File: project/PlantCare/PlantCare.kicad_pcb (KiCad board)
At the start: 4 copper layers, 45.5 x 22.5 mm, 41 parts, among them J1 TFT_0.96_13, J2 TTL-connect-pin4, J3 usbc, J4 Conn_01x02_Female, J5 Conn_01x01_Female, Q1 S8050, Q2 S8050, Q3 S8050, Q4 Q_NMOS_GSD, SW1 SW_DPDT_x2, SW2 SW_Push, SW3 SW_Push, U1 AMS1117-3.3, U2 ESP-12E, U3 CH340C

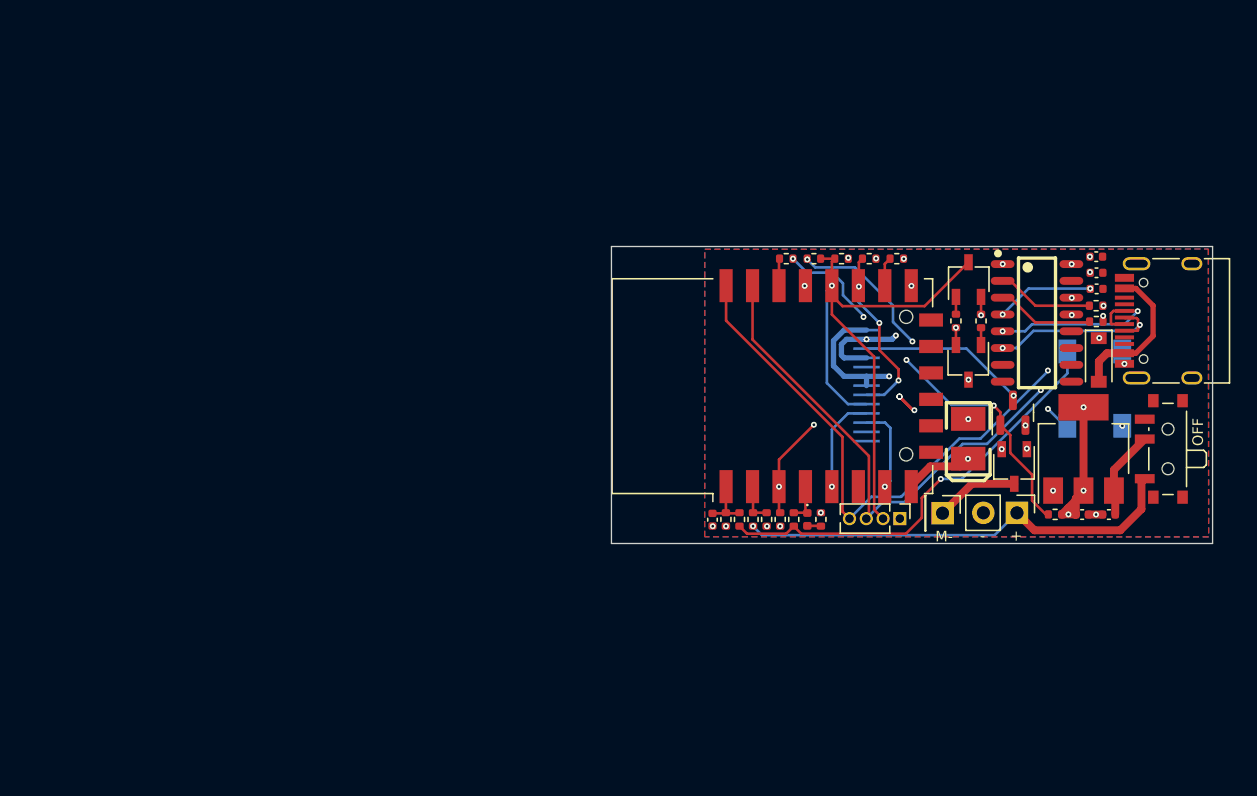
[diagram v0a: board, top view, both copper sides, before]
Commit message: update plant carer 1.2
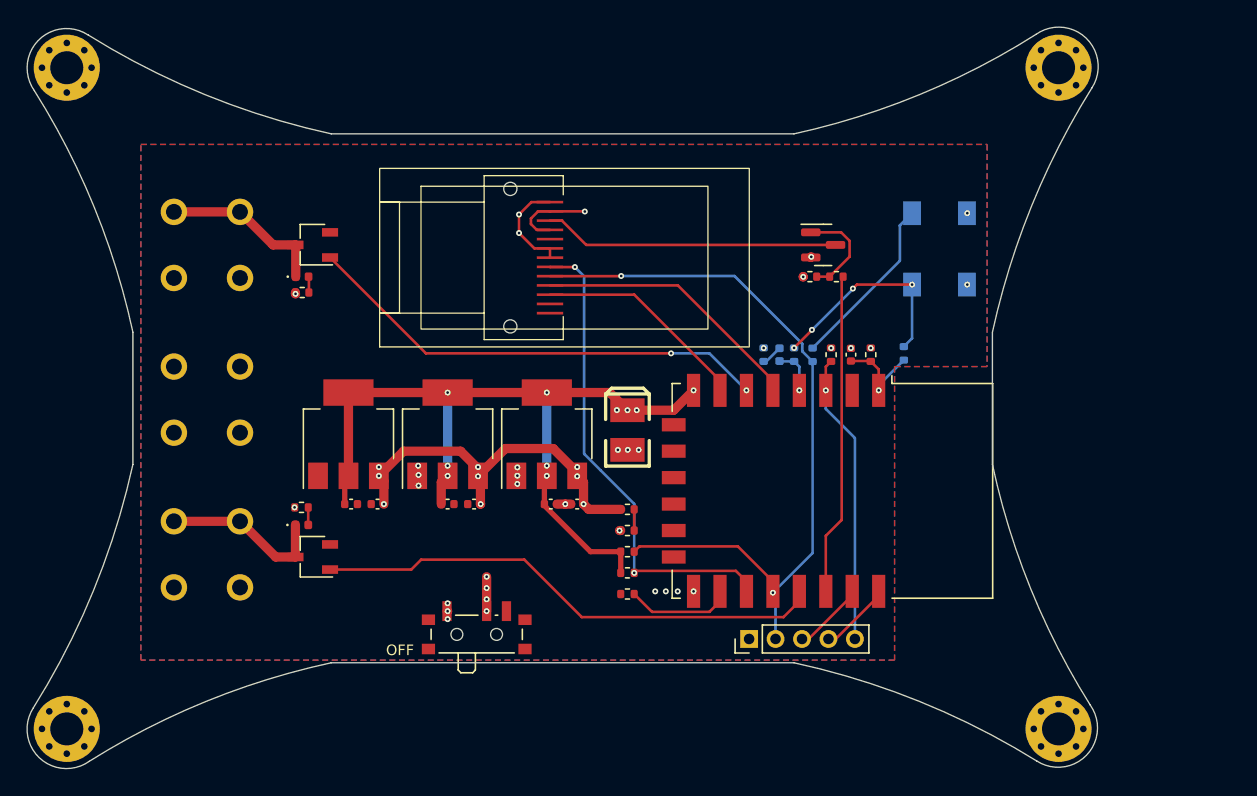
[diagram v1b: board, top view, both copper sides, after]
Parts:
- removed C5: 10uf, Capacitor_SMD:C_0402_1005Metric
- removed C6, C7: 100nf, Capacitor_SMD:C_0402_1005Metric
- removed Q3: S8050, Package_TO_SOT_SMD:TSOT-23
- removed R16: 100k, Resistor_SMD:R_0402_1005Metric
- removed R17: 330k, Resistor_SMD:R_0402_1005Metric
- removed U3: CH340C, lc_lib:SOP-16_150MIL
- added C10: 10uf, Capacitor_SMD:C_0402_1005Metric, F.Cu at (93.8, 108.0)
- added C11: 10uf, Capacitor_SMD:C_0402_1005Metric, F.Cu at (95.8, 108.0)
- added C8: 10uf, Capacitor_SMD:C_0402_1005Metric, F.Cu at (86.5, 108.0)
- added C9: 10uf, Capacitor_SMD:C_0402_1005Metric, F.Cu at (88.5, 108.0)
- added D3: led-white, LED_SMD:LED_0402_1005Metric, F.Cu at (82.8, 90.8)
- added H1: MountingHole, MountingHole:MountingHole_2.5mm_Pad_Via, F.Cu at (65.0, 75.0)
- added H2: MountingHole, MountingHole:MountingHole_2.5mm_Pad_Via, F.Cu at (140.0, 125.0)
- added H3: MountingHole, MountingHole:MountingHole_2.5mm_Pad_Via, F.Cu at (65.0, 125.0)
- added H4: MountingHole, MountingHole:MountingHole_2.5mm_Pad_Via, F.Cu at (140.0, 75.0)
- added U4: AMS1117-3.3, Package_TO_SOT_SMD:SOT-223-3_TabPin2, F.Cu at (86.3, 102.7)
- added U5: AMS1117-3.3, Package_TO_SOT_SMD:SOT-223-3_TabPin2, F.Cu at (93.8, 102.7)
- C2: value 1uf -> 10uf
- D1, R2, R5, R6, R7: moved to B.Cu
- D2: value B120-E3 -> led-white; footprint Diode_SMD:D_SOD-123 -> LED_SMD:LED_0402_1005Metric
- J1: moved to F.Cu
- J2: footprint Connector_PinHeader_1.27mm:PinHeader_1x04_P1.27mm_Vertical -> Connector_PinHeader_2.00mm:PinHeader_1x05_P2.00mm_Vertical
- J3: value usbc -> Conn_01x02_Female; footprint Connector_USB:USB_C_Receptacle_HRO_TYPE-C-31-M-12 -> My-lib-footprints:Connect_push_5mm
- J4: footprint Connector_PinHeader_2.54mm:PinHeader_1x02_P2.54mm_Vertical -> My-lib-footprints:Connect_push_5mm
- J5: value Conn_01x01_Female -> Conn_01x02_Female; footprint Connector_PinHeader_2.54mm:PinHeader_1x01_P2.54mm_Vertical -> My-lib-footprints:Connect_push_5mm
- Q2: value S8050 -> Q_NMOS_GSD
- R11, R12: value 470 -> 12K
- R14: value 12K -> 100k
- R15: value 12K -> 330k
- moved J3 73.7 mm to (75.6, 88.4), turned to -90 degrees
- moved R11 62.0 mm to (82.8, 108.2), turned to 0 degrees
- moved J4 61.9 mm to (75.6, 100.1), turned to 90 degrees
- moved D2 61.5 mm to (82.8, 109.6), turned to 0 degrees
- moved R12 60.1 mm to (82.8, 92.0)
- moved J5 55.7 mm to (75.6, 111.8)
- moved SW1 53.7 mm to (96.0, 117.5), turned to 0 degrees
- moved Q4 53.5 mm to (83.6, 112.0), turned to 180 degrees
- moved J1 50.6 mm to (88.7, 82.6)
- moved Q2 50.4 mm to (83.6, 88.4), turned to 180 degrees
- moved C2 42.2 mm to (101.6, 108.0), turned to 0 degrees
- moved U1 40.6 mm to (101.3, 102.7)
- moved C3 38.2 mm to (103.6, 108.0), turned to 180 degrees
- moved R9 32.5 mm to (107.4, 114.8), turned to 180 degrees
- moved R14 31.1 mm to (107.4, 110.0), turned to 0 degrees
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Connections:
- C2 pad 1: Net-(C2-Pad1) -> +3V3
- C3 pad 1: +3V3 -> Net-(C11-Pad1)
- D2 pad 1: Net-(C5-Pad1) -> /control
- Q2 pad 1: Net-(Q2-Pad1) -> /GPIO12
- Q2 pad 2: Net-(Q2-Pad2) -> GND
- Q2 pad 3: /EN -> /control1
- R11 pad 1: /RXD -> +BATT
- R11 pad 2: Net-(R11-Pad2) -> Net-(D2-Pad2)
- R12 pad 1: Net-(R12-Pad1) -> +BATT
- R12 pad 2: /TXD -> Net-(D3-Pad2)
- R14 pad 1: Net-(Q2-Pad1) -> GND
- R14 pad 2: Net-(Q3-Pad2) -> /POWER/ADC
- R15 pad 1: Net-(Q3-Pad1) -> /POWER/ADC
- R15 pad 2: Net-(Q2-Pad2) -> Net-(C11-Pad1)
- SW1 pad 2: Net-(C2-Pad1) -> Net-(C11-Pad1)
- U1 pad 3: Net-(C2-Pad1) -> Net-(C11-Pad1)
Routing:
- net +3V3: track 25.6 -> 69.4 mm, vias 11 -> 15
- net /TXD: track 47.5 -> 5.50 mm, vias 2 -> 0
- net /RXD: track 47.0 -> 5.47 mm, vias 2 -> 0
- net /GPIO12: track 0.00 -> 35.7 mm, vias 0 -> 2
- net +BATT: track 34.1 -> 0.16 mm, vias 1 -> 5
- net Net-(C11-Pad1): track 0.00 -> 31.2 mm, vias 0 -> 13
- net /GPIO2: track 13.4 -> 36.5 mm, vias 3 -> 2
- net Net-(Q1-Pad1): track 30.5 -> 7.52 mm, vias 4 -> 0
- net /GPIO5: track 2.06 -> 24.3 mm
- net Net-(R5-Pad2): track 33.1 -> 15.9 mm, vias 1 -> 4
- net Net-(J3-PadA6): track 14.8 -> 0.00 mm, vias 2 -> 0
- net Net-(J3-PadA7): track 14.3 -> 0.00 mm, vias 2 -> 0
- net /GPIO14: track 7.45 -> 20.6 mm, vias 1 -> 0
- net /control1: track 0.00 -> 12.6 mm
- net Net-(C5-Pad1): track 12.4 -> 0.00 mm, vias 4 -> 0
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- added copper zone on In2.Cu, net +BATT
- added copper zone on In2.Cu, net Net-(C11-Pad1)
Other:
- board size 45.5 x 22.5 mm -> 81 x 56.1 mm
- board text added: "CON1"
- board text added: "CON2"
- board text added: "EN"
- board text added: "GND"
- board text added: "POWER"
- board text added: "Plant Carer V1.2"
- board text added: "RXD"
- board text added: "TXD"
- board text removed: "+"
- board text removed: "-"
- board text removed: "FLASH"
- board text removed: "G"
- board text removed: "M-"
- board text removed: "RST"
- board text removed: "RX"
- board text removed: "TX"
